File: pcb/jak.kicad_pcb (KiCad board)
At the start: 2 copper layers, 230.7 x 96.9 mm, 94 parts, among them SW1 SW_Push, SW10 SW_Push, SW10_r1 SW_Push, SW11 SW_Push, SW11_r1 SW_Push, SW12 SW_Push, SW12_r1 SW_Push, SW13 SW_Push, SW13_r1 SW_Push, SW14 SW_Push, SW14_r1 SW_Push, SW15 SW_Push, SW15_r1 SW_Push, SW16 SW_Push, SW16_r1 SW_Push, SW17 SW_Push, SW17_r1 SW_Push, SW18 SW_Push, SW18_r1 SW_Push, SW1_r1 SW_Push, SW2 SW_Push, SW2_r1 SW_Push, SW3 SW_Push, SW3_r1 SW_Push, SW4 SW_Push, SW4_r1 SW_Push, SW5 SW_Push, SW5_r1 SW_Push, SW6 SW_Push, SW6_r1 SW_Push, SW7 SW_Push, SW7_r1 SW_Push, SW8 SW_Push, SW8_r1 SW_Push, SW9 SW_Push, SW9_r1 SW_Push

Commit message: tt
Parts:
- controller1, controller_r1: value ProMicro -> ProMicro_r
- jst1, jst2, jst_r1, jst_r2: footprint project:2-pin-jst -> jak:2-pin-jst
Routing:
- net GND_r: vias 0 -> 1
- net (no net): vias 1 -> 0

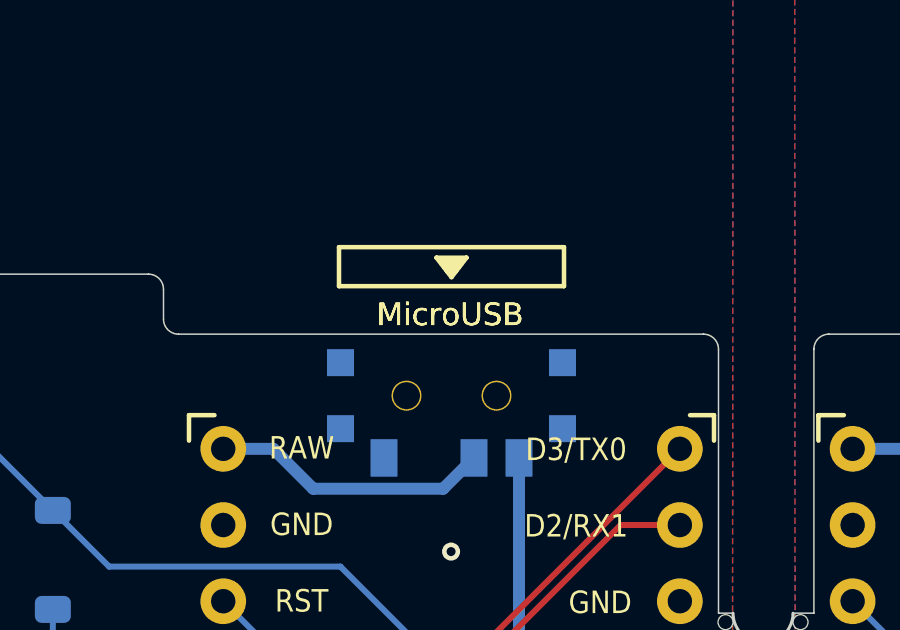
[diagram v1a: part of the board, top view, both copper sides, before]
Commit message: Fixed the submodule issus for the symbol and footprint libraries
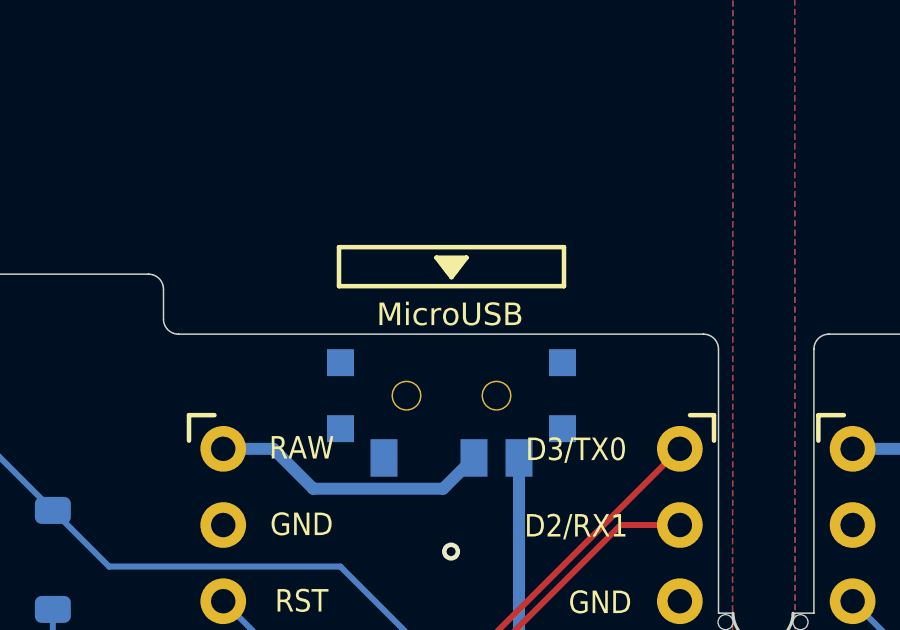
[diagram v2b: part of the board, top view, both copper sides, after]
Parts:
- controller1, controller_r1: value ProMicro_r -> ProMicro
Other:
- board text removed: "MicroUSB"
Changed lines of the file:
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@@
 			)
 		)
-		(property "Value" "ProMicro_r"
+		(property "Value" "ProMicro"
 			(at -0.1 0.05 90)
 			(layer "F.Fab")
@@
 			)
 		)
-		(fp_text user "MicroUSB"
-			(at -0.05 -18.95 0)
-			(layer "F.SilkS")
-			(effects
-				(font
-					(size 0.75 0.75)
-					(thickness 0.12)
-				)
-			)
-		)
 		(fp_text user "RAW"
 			(at -4.995 -14.5 0)
@@
 			)
 		)
-		(property "Value" "ProMicro_r"
+		(property "Value" "ProMicro"
 			(at -0.1 0.05 90)
 			(layer "F.Fab")
@@
 			)
 		)
-		(fp_text user "MicroUSB"
-			(at -0.05 -18.95 0)
-			(layer "F.SilkS")
-			(effects
-				(font
-					(size 0.75 0.75)
-					(thickness 0.12)
-				)
-			)
-		)
 		(fp_text user "15/B1"
 			(at -4.395 5.85 0)
@@
 		)
 	)
-	(gr_text "MicroUSB"
-		(at 135.963859 61.603 0)
-		(layer "F.SilkS")
-		(effects
-			(font
-				(size 0.75 0.75)
-				(thickness 0.12)
-			)
-		)
-	)

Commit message: In the process of transitioning the board to use the SEEED XIAO instead of a pro micro
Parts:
- removed the REF** at (147.5, 121.5)
- removed the REF** at (147.4, 73.6)
- removed RSW1, RSW2: SW_Push, kbd:ResetSW
- removed jst2, jst_r2: Conn_01x02, jak:2-pin-jst
- added REF**: MouseBite-Slot_2.0x2.0mm_outset_D0.5mm_P0.85mm_3h, Panelization:MouseBite-Slot_2.0x2.0mm_outset_D0.5mm_P0.85mm_3h, F.Cu at (147.6, 120.0)
- added REF**: MouseBite-Slot_2.0x2.0mm_outset_D0.5mm_P0.85mm_3h, Panelization:MouseBite-Slot_2.0x2.0mm_outset_D0.5mm_P0.85mm_3h, F.Cu at (147.6, 103.0)
- added RES1: PTS526 SM15 SMTR2 LFS, footprints:SON4_PTS526 SM15 SMTR2 LFS_CNK, B.Cu at (130.1, 111.4)
- added RES_r1: PTS526 SM15 SMTR2 LFS, footprints:SON4_PTS526 SM15 SMTR2 LFS_CNK, B.Cu at (163.1, 111.4)
- controller1, controller_r1: value ProMicro -> XIAO-nRF52840-SMD; footprint kbd:ProMicro -> jak:XIAO-nRF52840-SMD-underside; moved to B.Cu
- jst1: footprint jak:2-pin-jst -> S2B-PH-K-S_LF__SN_:JST_S2B-PH-K-S_LF__SN_; moved to B.Cu
- jst_r1: value Conn_01x02 -> S2B-PH-K-S_LF__SN_; footprint jak:2-pin-jst -> S2B-PH-K-S_LF__SN_:JST_S2B-PH-K-S_LF__SN_; moved to B.Cu
- power1, power_r1: footprint Kicad-Footprints:SPDT_C128955 -> Button_Switch_SMD:SW_SPDT_PCM12
- moved power1 61.5 mm to (141.3, 125.5), turned to -120 degrees
- moved power_r1 61.4 mm to (151.9, 125.5), turned to 120 degrees
- moved jst1 25.2 mm to (125.2, 120.3), turned to 90 degrees
- moved jst_r1 23.7 mm to (167.9, 120.3), turned to -90 degrees
- moved controller_r1 12.3 mm to (157.1, 92.8), turned to 180 degrees
- moved controller1 12.3 mm to (136.0, 92.8), turned to 180 degrees
- moved D17 4.40 mm to (113.6, 127.0)
- moved split_connector1 1.22 mm to (143.9, 111.5)
- moved split_connector_r1 1.15 mm to (149.3, 111.5)
- moved SW18 1.09 mm to (127.1, 135.3)
- moved D12 1.09 mm to (65.7, 104.8)
- moved D13 1.09 mm to (84.8, 98.8)
- moved D14 1.09 mm to (103.8, 104.3)
- moved D2 1.09 mm to (65.7, 66.7)
- moved D4 1.09 mm to (103.8, 66.2)
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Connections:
- controller1 pad 1: split_comms+ -> row0
- controller1 pad 10: row3 -> col3
- controller1 pad 11: unconnected-(controller1-8/B4-Pad11) -> col4
- controller1 pad 12: unconnected-(controller1-9/B5-Pad12) -> VCC
- controller1 pad 13: unconnected-(controller1-B6/10-Pad13) -> GND
- controller1 pad 15: col0 -> battery_switched
- controller1 pad 16: col1 -> GND
- controller1 pad 2: split_comms- -> row1
- controller1 pad 21: VCC -> reset
- controller1 pad 22: reset -> GND
- controller1 pad 3: GND -> row2
- controller1 pad 4: GND -> row3
- controller1 pad 5: unconnected-(controller1-2/D1/SDA-Pad5) -> col1
- controller1 pad 6: unconnected-(controller1-3/D0/SCL-Pad6) -> col0
- controller1 pad 7: row0 -> split_comms+
- controller1 pad 8: row1 -> split_comms-
- controller1 pad 9: row2 -> col2
- controller_r1 pad 1: split_comms-_r -> row0_r
- controller_r1 pad 10: row3_r -> col3_r
- controller_r1 pad 11: unconnected-(controller_r1-8/B4-Pad11) -> col4_r
- controller_r1 pad 12: unconnected-(controller_r1-9/B5-Pad12) -> VCC_r
- controller_r1 pad 13: unconnected-(controller_r1-B6/10-Pad13) -> GND_r
- controller_r1 pad 15: col0_r -> battery_switched_r
- controller_r1 pad 16: col1_r -> GND_r
- controller_r1 pad 2: split_comms+_r -> row1_r
- controller_r1 pad 21: VCC_r -> reset_r
- controller_r1 pad 22: reset_r -> GND_r
- controller_r1 pad 3: GND_r -> row2_r
- controller_r1 pad 4: GND_r -> row3_r
- controller_r1 pad 5: unconnected-(controller_r1-2/D1/SDA-Pad5) -> col1_r
- controller_r1 pad 6: unconnected-(controller_r1-3/D0/SCL-Pad6) -> col0_r
- controller_r1 pad 7: row0_r -> split_comms-_r
- controller_r1 pad 8: row1_r -> split_comms+_r
- controller_r1 pad 9: row2_r -> col2_r
- power1 pad 2: raw -> battery_switched
- power_r1 pad 1: unconnected-(power_r1-A-Pad1) -> battery+_r
- power_r1 pad 2: raw_r -> battery_switched_r
- power_r1 pad 3: battery+_r -> unconnected-(power_r1-C-Pad3)
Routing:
- net battery_switched: track 0.00 -> 37.3 mm
- net split_comms-_r: track 54.8 -> 19.0 mm, vias 1 -> 2
- net battery_switched_r: track 0.00 -> 34.6 mm
- net split_comms+: track 55.8 -> 21.3 mm, vias 1 -> 0
- net split_comms-: track 52.6 -> 19.7 mm, vias 3 -> 4
- net split_comms+_r: track 50.2 -> 17.4 mm
- net battery+_r: track 40.1 -> 16.0 mm, vias 1 -> 0
- net battery+: track 40.3 -> 16.8 mm, vias 1 -> 0
- net col0_r: track 143.1 -> 124.3 mm, vias 3 -> 5
- net VCC_r: track 50.9 -> 32.2 mm, vias 2 -> 0
- net col1_r: track 121.3 -> 104.0 mm, vias 3 -> 5
- net VCC: track 48.0 -> 32.9 mm, vias 2 -> 5
- net col1: track 121.7 -> 136.4 mm, vias 3 -> 5
- net row3: track 82.6 -> 95.7 mm
- net col0: track 144.8 -> 157.2 mm, vias 0 -> 2
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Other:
- board size 230.7 x 96.9 mm -> 230.5 x 96.9 mm
- board text removed: "+"
- board text removed: "-"

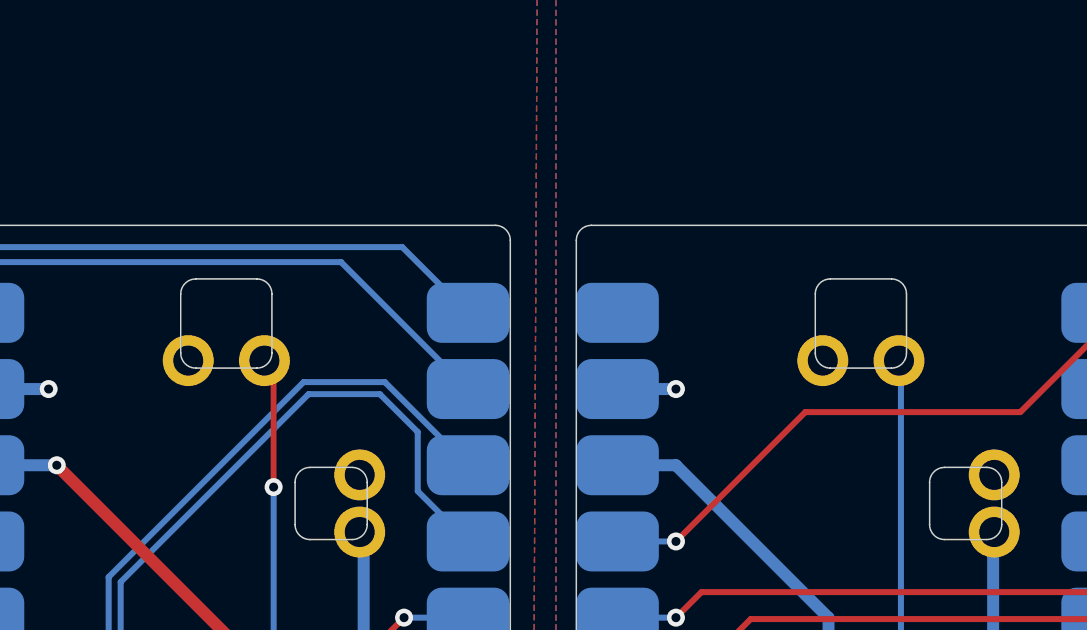
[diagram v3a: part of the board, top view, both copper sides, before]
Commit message: Made some final changes to the pcb and split the switch plate into two versions to allow metal decorations
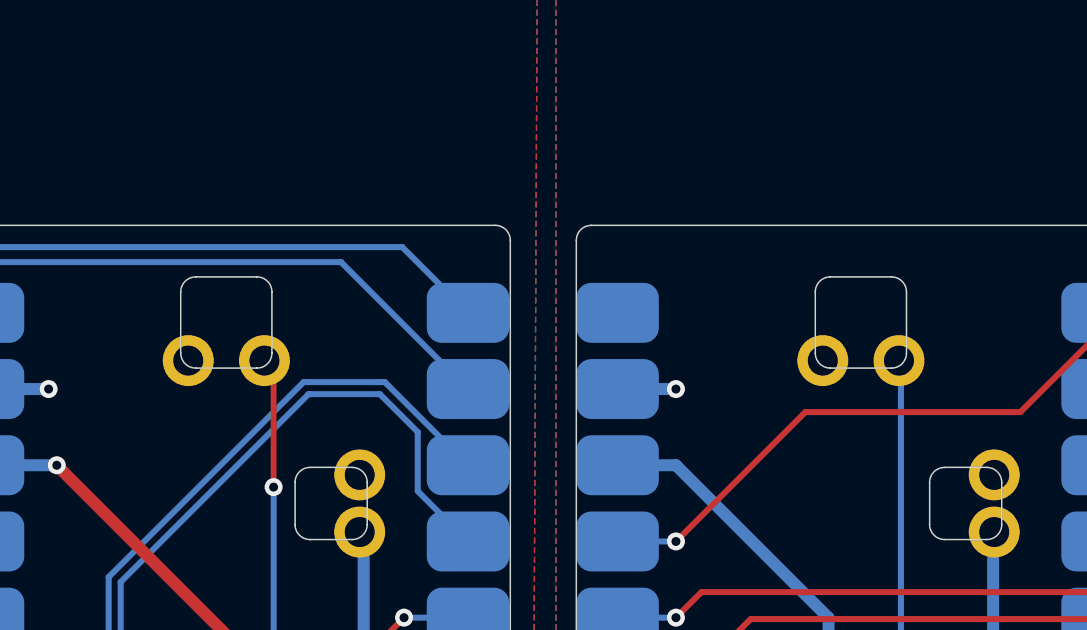
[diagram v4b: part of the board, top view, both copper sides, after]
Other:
- board text added: "+"
- board text added: "-"
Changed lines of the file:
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@@
 			(layer "F.SilkS"
 				(type "Top Silk Screen")
+				(color "White")
 			)
 			(layer "F.Paste"
@@
 			(layer "B.SilkS"
 				(type "Bottom Silk Screen")
+				(color "White")
 			)
 			(copper_finish "None")
@@
 			(plot_on_all_layers_selection 0x00000000_00000000_00000000_00000000)
 			(disableapertmacros no)
-			(usegerberextensions no)
+			(usegerberextensions yes)
 			(usegerberattributes yes)
 			(usegerberadvancedattributes yes)
-			(creategerberjobfile yes)
+			(creategerberjobfile no)
 			(dashed_line_dash_ratio 12.000000)
 			(dashed_line_gap_ratio 3.000000)
@@
 			(outputformat 1)
 			(mirror no)
-			(drillshape 1)
+			(drillshape 0)
 			(scaleselection 1)
-			(outputdirectory "")
+			(outputdirectory "gerbers/")
 		)
 	)
@@
 		)
 		(fp_line
-			(start 1.465 8.25)
+			(start 1.465 8.3185)
 			(end 1.465 6.2785)
 			(stroke
@@
 		)
 		(fp_line
-			(start -1.075 8.75)
-			(end 0.965 8.75)
+			(start -1.075 8.8185)
+			(end 0.965 8.8185)
 			(stroke
 				(width 0.05)
@@
 		(fp_line
 			(start -1.575 6.2785)
-			(end -1.575 8.25)
+			(end -1.575 8.3185)
 			(stroke
 				(width 0.05)
@@
 		)
 		(fp_arc
-			(start 1.465 8.25)
-			(mid 1.318553 8.603553)
-			(end 0.965 8.75)
+			(start 1.465 8.3185)
+			(mid 1.318553 8.672053)
+			(end 0.965 8.8185)
 			(stroke
 				(width 0.05)
@@
 		)
 		(fp_arc
-			(start -1.075 8.75)
-			(mid -1.428553 8.603553)
-			(end -1.575 8.25)
+			(start -1.075 8.8185)
+			(mid -1.428553 8.672053)
+			(end -1.575 8.3185)
 			(stroke
 				(width 0.05)
@@
 		)
 		(fp_line
-			(start 1.465 8.25)
+			(start 1.465 8.3185)
 			(end 1.465 6.2785)
 			(stroke
@@
 		)
 		(fp_line
-			(start -1.075 8.75)
-			(end 0.965 8.75)
+			(start -1.075 8.8185)
+			(end 0.965 8.8185)
 			(stroke
 				(width 0.05)
@@
 		(fp_line
 			(start -1.575 6.2785)
-			(end -1.575 8.25)
+			(end -1.575 8.3185)
 			(stroke
 				(width 0.05)
@@
 		)
 		(fp_arc
-			(start 1.465 8.25)
-			(mid 1.318553 8.603553)
-			(end 0.965 8.75)
+			(start 1.465 8.3185)
+			(mid 1.318553 8.672053)
+			(end 0.965 8.8185)
 			(stroke
 				(width 0.05)
@@
 		)
 		(fp_arc
-			(start -1.075 8.75)
-			(mid -1.428553 8.603553)
-			(end -1.575 8.25)
+			(start -1.075 8.8185)
+			(mid -1.428553 8.672053)
+			(end -1.575 8.3185)
 			(stroke
 				(width 0.05)
@@
 			(at -2.375 9.045 270)
 			(layer "B.SilkS")
+			(hide yes)
 			(effects
 				(font
@@
 		(at 167.944 120.275 -90)
 		(property "Reference" "jst_r1"
-			(at -0.55 -2.7125 90)
+			(at 0.225 -5.056 90)
 			(layer "B.SilkS")
 			(effects
@@
 		(at 125.2145 120.275 90)
 		(property "Reference" "jst1"
-			(at 0 -2.7125 90)
+			(at 0 -4.7145 90)
 			(layer "B.SilkS")
 			(effects
@@
 		(layer "Edge.Cuts")
 	)
+	(gr_text "-"
+		(at 169.403119 118.717165 180)
+		(layer "B.SilkS")
+		(effects
+			(font
+				(size 1 1)
+				(thickness 0.1)
+			)
+			(justify left bottom mirror)
+		)
+	)
+	(gr_text "+"
+		(at 123.880283 119.687203 0)
+		(layer "B.SilkS")
+		(effects
+			(font
+				(size 1 1)
+				(thickness 0.1)
+			)
+			(justify left bottom mirror)
+		)
+	)
+	(gr_text "+"
+		(at 169.455695 120.859616 180)
+		(layer "B.SilkS")
+		(effects
+			(font
+				(size 1 1)
+				(thickness 0.1)
+			)
+			(justify left bottom mirror)
+		)
+	)
+	(gr_text "-"
+		(at 123.932859 121.829654 0)
+		(layer "B.SilkS")
+		(effects
+			(font
+				(size 1 1)
+				(thickness 0.1)
+			)
+			(justify left bottom mirror)
+		)
+	)
 	(segment
 		(start 138.900584 126.769519)
@@
 		)
 	)
+	(group ""
+		(members "2b0de856-dfc9-4e91-8a52-c332b3e26ac7" "75c2403c-2e76-48d7-a2bc-6bf307c04ec1")
+	)
+	(group ""
+		(members "29fda440-a156-4d26-a06a-1eef97d3202f" "4ad15358-b984-4096-822e-b9add0e3d5e0")
+	)
 	(embedded_fonts no)
